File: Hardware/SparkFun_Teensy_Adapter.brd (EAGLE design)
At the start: 18 parts, among them J1 ARDUINO_R3_SHIELDUNO_R3_SHIEL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, J2 AVR_SPI_PRG_6PTH, U1 TEENSY-3.1

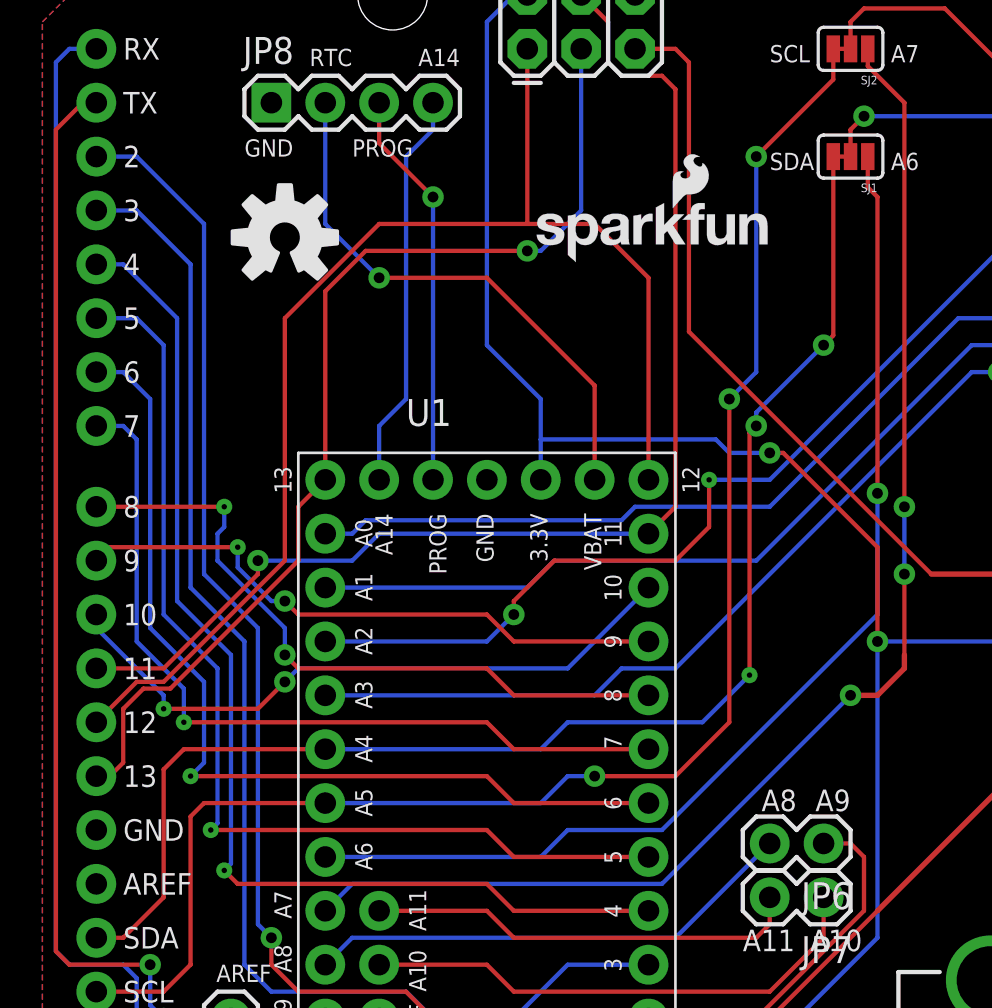
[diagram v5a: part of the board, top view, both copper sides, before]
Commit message: Fixing additional DRC errors, adding in board name to silk
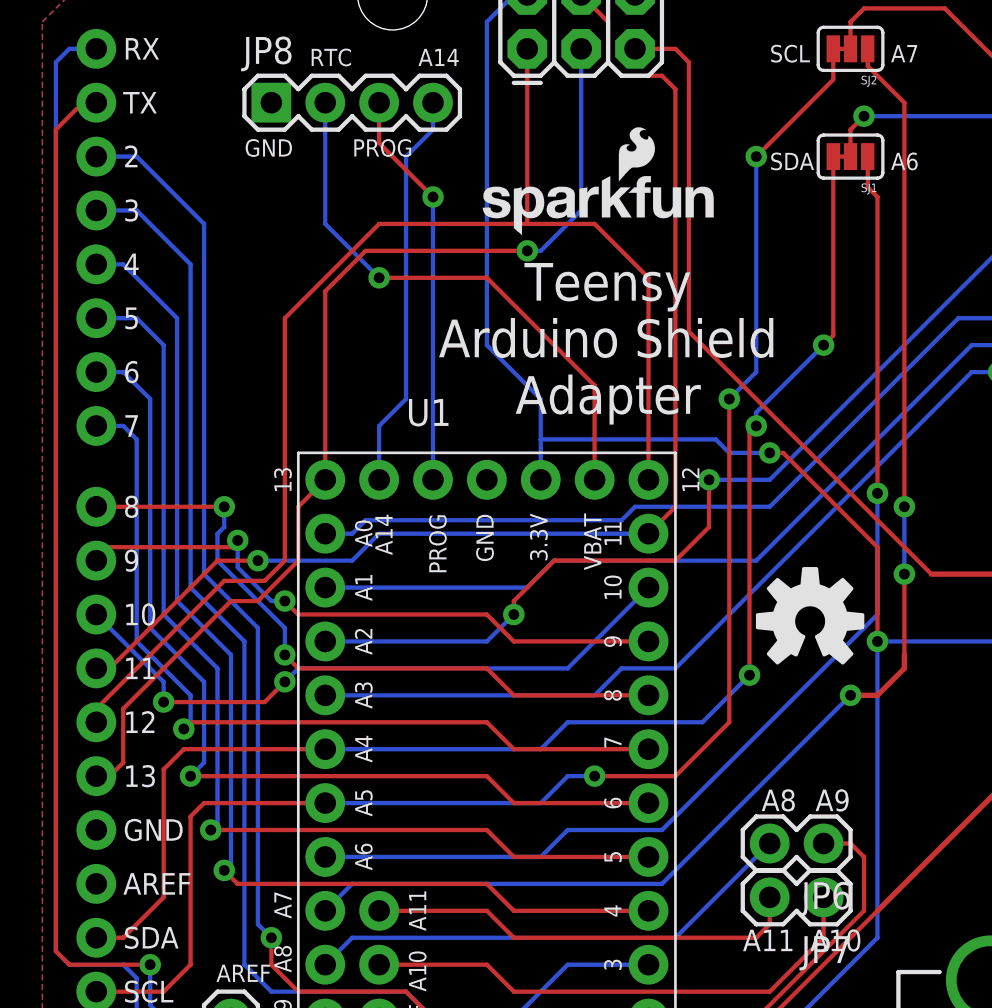
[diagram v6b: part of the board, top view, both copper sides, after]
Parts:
- moved LOGO2 30.7 mm to (38.7, 44.1)
- moved LOGO1 2.84 mm to (22.9, 62.2)
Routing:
- net D7: track 38.9 -> 39.6 mm
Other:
- board text added: "Teensy Arduino Shield Adapter"

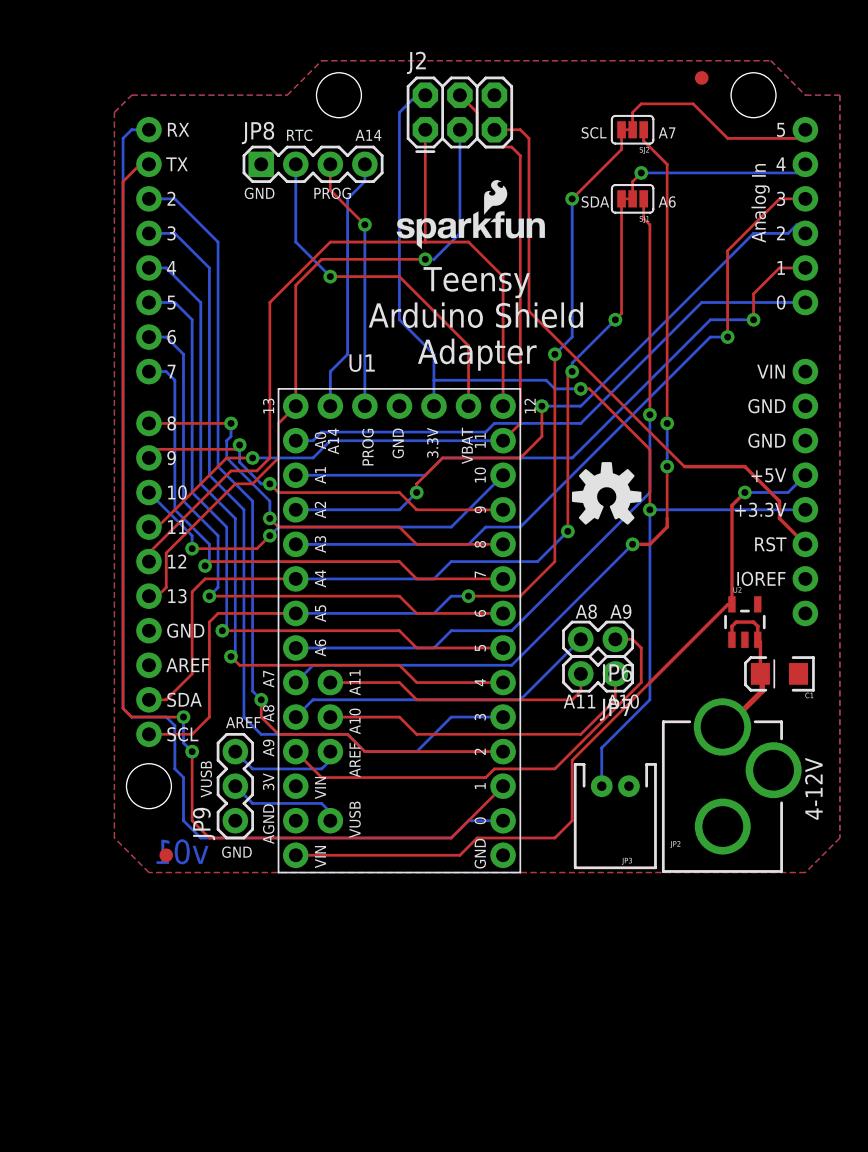
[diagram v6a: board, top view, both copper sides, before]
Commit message: Adding switch for USB Host, RTC battery holder
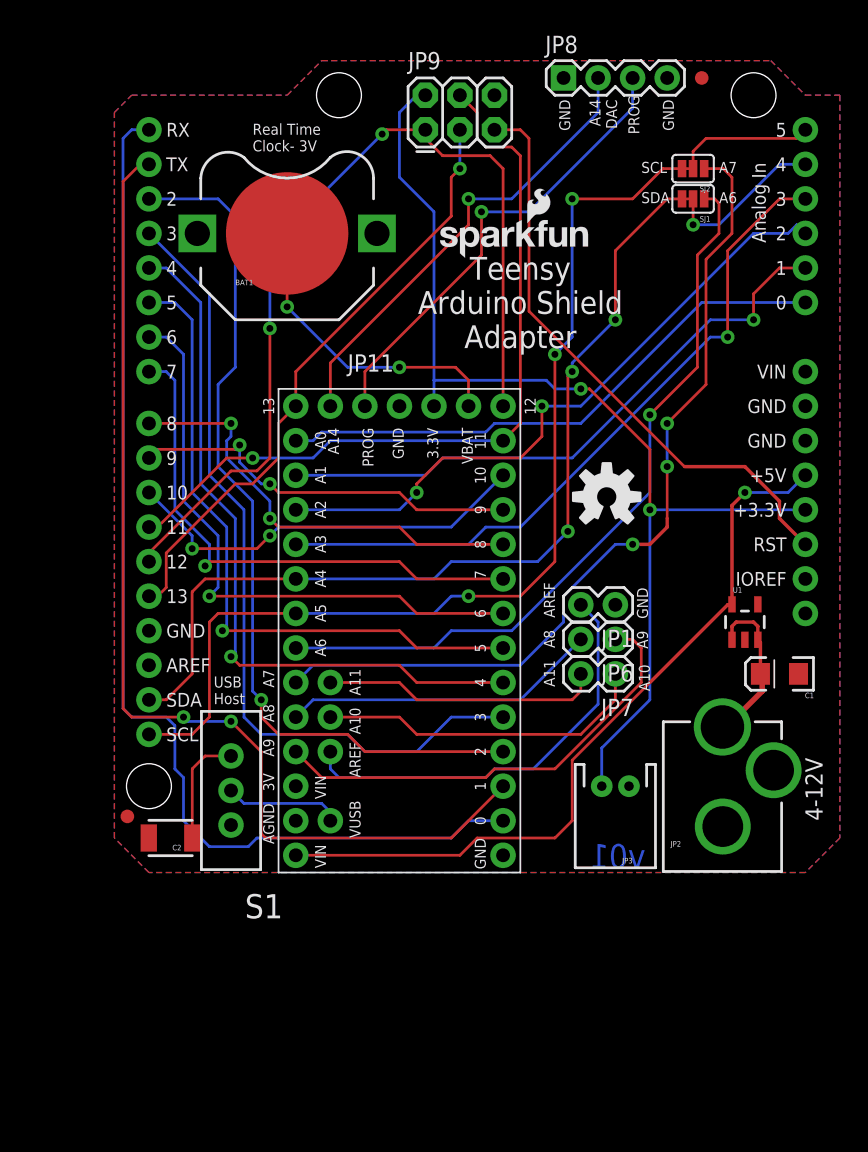
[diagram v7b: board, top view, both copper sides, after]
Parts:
- removed J2: AVR_SPI_PRG_6PTH, SparkFun-Connectors:2X3
- removed U2: (no value), SparkFun-PowerIC:SOT23-5
- added BAT1: (no value), SparkFun-Electromechanical:BATTCON_12MM_PTH
- added C2: 100uF, SparkFun-Capacitors:1210
- added JP1: M02PTH, SparkFun-Connectors:1X02
- added JP11: TEENSY-3.1, Testing:TEENSY-3.1
- added S1: (no value), SparkFun-Electromechanical:SWITCH-SPDT
- JP9: value (none) -> AVR_SPI_PRG_6PTH; device SparkFun-Connectors:1X03 -> SparkFun-Connectors:2X3
- U1: value TEENSY-3.1 -> (none); device Testing:TEENSY-3.1 -> SparkFun-PowerIC:SOT23-5
- moved JP9 52.7 mm to (25.4, 71.1), turned to 0 degrees
- moved U1 38.9 mm to (48.9, 34.9)
- moved JP8 23.1 mm to (35.6, 74.9)
- moved SJ2 5.28 mm to (45.1, 68.3)
- moved SJ1 4.45 mm to (45.1, 66.0)
- moved FID2 4.04 mm to (3.49, 20.6)
- moved LOGO1 3.24 mm to (26.0, 61.6)
- renumbered J1 to JP10
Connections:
- new net N$1: C2.1, S1.3
- net 3.3V: now also JP11.3.3V, JP9.2; no longer J2.2, U1.3.3V
- net 5V: now also JP11.VIN, U1.5; no longer U1.VIN, U2.5
- net A0: now also JP11.14; no longer U1.14
- net A1: now also JP11.15; no longer U1.15
- net A10: now also JP11.A10; no longer U1.A10
- net A11: now also JP11.A11; no longer U1.A11
- net A14/DAC: now also JP11.A14/DAC, JP8.2; no longer JP8.4, U1.A14/DAC
- net A2: now also JP11.16; no longer U1.16
- net A3: now also JP11.17; no longer U1.17
- net A6: now also JP11.20; no longer U1.20
- net A7: now also JP11.21; no longer U1.21
- net A8: now also JP11.22; no longer U1.22
- net A9: now also JP11.23; no longer U1.23
- net AREF: now also JP1.2, JP11.AREF; no longer JP9.3, U1.AREF
- net CS: now also JP11.10; no longer U1.10
- net D2: now also JP11.2; no longer U1.2
- net D3: now also JP11.3; no longer U1.3
- net D4: now also JP11.4; no longer U1.4
- net D5: now also JP11.5; no longer U1.5
- net D6: now also JP11.6; no longer U1.6
- net D7: now also JP11.7; no longer U1.7
- net D8: now also JP11.8; no longer U1.8
- net D9: now also JP11.9; no longer U1.9
- net GND: now also BAT1.VCC@1, C2.2, JP1.1, JP11.AGND, JP11.GND, JP11.GND1, JP8.4, JP9.6, U1.2; no longer J2.6, JP9.1, U1.AGND, U1.GND, U1.GND1, U2.2
- net MISO: now also JP11.12, JP9.1; no longer J2.1, U1.12
- net MOSI: now also JP11.11, JP9.4; no longer J2.4, U1.11
- net PROG: now also JP11.PROG; no longer U1.PROG
- net RESET: now also JP9.5; no longer J2.5
- net RTC_BATT: now also BAT1.GND, JP11.VBAT; no longer JP8.2, U1.VBAT
- net RX: now also JP11.0; no longer U1.0
- net SCK: now also JP11.13, JP9.3; no longer J2.3, U1.13
- net SCL: now also JP11.19; no longer U1.19
- net SDA: now also JP11.18; no longer U1.18
- net TX: now also JP11.1; no longer U1.1
- net VRAW: now also U1.1, U1.3; no longer U2.1, U2.3
- net VUSB: now also JP11.VUSB, S1.2; no longer JP9.2, U1.VUSB
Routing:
- net AREF: track 8.41 -> 31.3 mm
- net PROG: track 18.8 -> 34.3 mm
- net A14/DAC: track 18.8 -> 34.1 mm, vias 0 -> 1
- net N$1: track 0.00 -> 8.33 mm
- net MISO: track 61.7 -> 67.7 mm, vias 0 -> 2
- net A5: track 15.5 -> 10.2 mm
- net SCK: track 49.7 -> 44.9 mm
- net RTC_BATT: track 26.0 -> 22.9 mm, vias 1 -> 2
- net D2: track 61.5 -> 64.4 mm
- net A6: track 52.5 -> 55.4 mm
- net A4: track 14.5 -> 12.0 mm
- net SDA: track 65.5 -> 68.0 mm
- net SCL: track 73.0 -> 75.4 mm
- net A7: track 62.0 -> 63.2 mm
- net D3: track 60.7 -> 59.6 mm
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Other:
- board text added: "A14 DAC"
- board text added: "Real Time Clock- 3V"
- board text added: "USB Host"
- board text removed: "A14"
- board text removed: "RTC"
- board text removed: "VUSB"

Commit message: Swapping to all PTH parts, fixing name silk
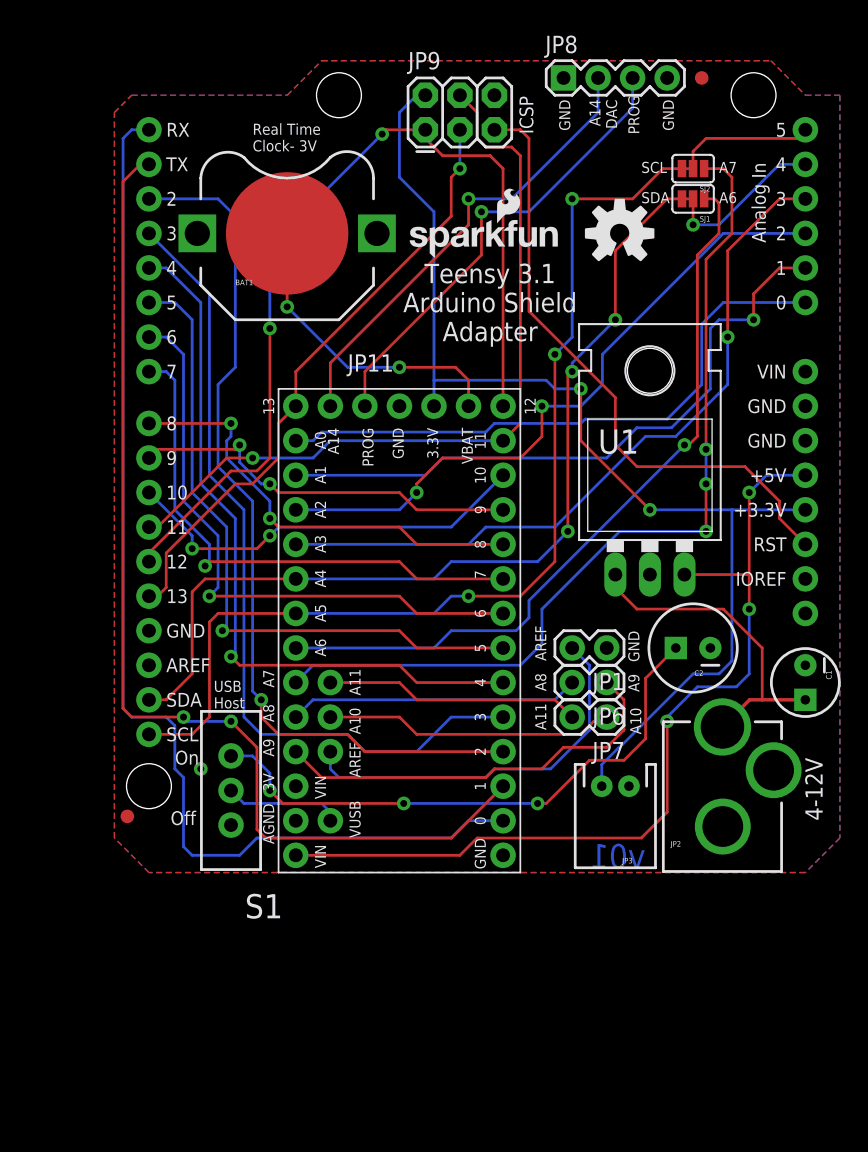
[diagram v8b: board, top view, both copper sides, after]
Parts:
- C1: device SparkFun-Capacitors:EIA3216 -> SparkFun-Capacitors:CPOL-RADIAL-10UF-25V
- C2: device SparkFun-Capacitors:1210 -> SparkFun-Capacitors:CPOL-RADIAL-100UF-25V
- U1: value (none) -> 5V; device SparkFun-PowerIC:SOT23-5 -> SparkFun-PowerIC:TO-220-ALT
- moved C2 40.9 mm to (45.1, 33.0)
- moved LOGO2 19.4 mm to (39.7, 63.5)
- moved U1 10.1 mm to (41.9, 42.2)
- moved JP6 3.24 mm to (38.7, 30.5)
- moved JP1 3.24 mm to (38.7, 33.0)
- moved JP7 3.24 mm to (38.7, 27.9)
- moved LOGO1 2.22 mm to (23.8, 61.6)
- moved C1 2.01 mm to (53.3, 30.5), turned to 270 degrees
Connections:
- net 5V: now also U1.OUT; no longer U1.5
- net GND: now also C1.2, U1.GND; no longer C1.C, U1.2
- net VRAW: now also C1.1, U1.IN; no longer C1.A, U1.1, U1.3
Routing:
- net N$1: track 8.33 -> 42.2 mm, vias 0 -> 3
- net VRAW: track 12.1 -> 24.3 mm
- net 5V: track 55.9 -> 65.7 mm, vias 1 -> 3
- net A9: track 33.8 -> 30.4 mm
- net 3.3V: track 80.7 -> 84.0 mm
- net A10: track 24.4 -> 21.4 mm
- net AREF: track 31.3 -> 28.6 mm
- net A1: track 44.9 -> 47.5 mm
- net A0: track 41.7 -> 44.3 mm
- net A7: track 63.2 -> 65.4 mm
- net RESET: track 43.7 -> 45.7 mm
- net A3: track 51.7 -> 53.8 mm
- net A8: track 23.3 -> 21.4 mm
- net A11: track 20.5 -> 18.8 mm
- net RX: track 80.7 -> 82.4 mm
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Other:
- board text added: "ICSP"
- board text added: "Off"
- board text added: "On"
- board text added: "Teensy 3.1 Arduino Shield Adapter"
- board text removed: "Teensy Arduino Shield Adapter"
